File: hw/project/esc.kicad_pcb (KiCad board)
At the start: 4 copper layers, 183 parts, among them J1 Battery, J10 I2C, J11 Voltage Monitor, J12 Misc, J2 Phases, J3 FTSH-107-01-L-DV-K-A, J4 Throttle, J5 Hall, J6 Serial, J7 SPI, J8 2.54 Comm, J9 CAN, Q1 SQM50061EL_GE3, Q2 SQM50061EL_GE3, Q3 STL110N10F7, Q4 STL110N10F7, Q5 STL110N10F7, Q6 STL110N10F7, Q7 STL110N10F7, Q8 STL110N10F7, SW1 BOOT0, SW2 RESET, SW3 USER, U1 STSPIN32G4, U2 LMR51610XDBVR, U3 ATA6561-GAQW-N, X1 32MHZ 10PF

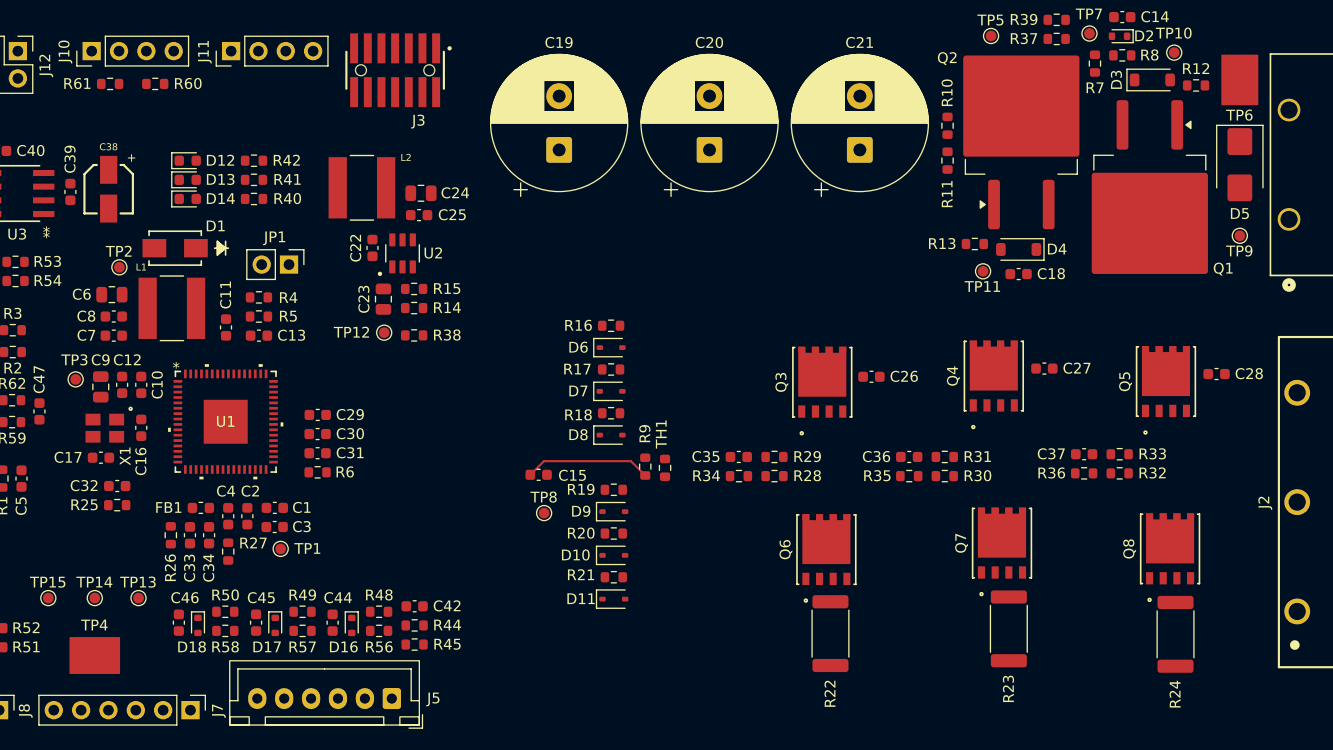
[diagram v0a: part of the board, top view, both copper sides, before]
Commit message: Rough draft layout for mosfets
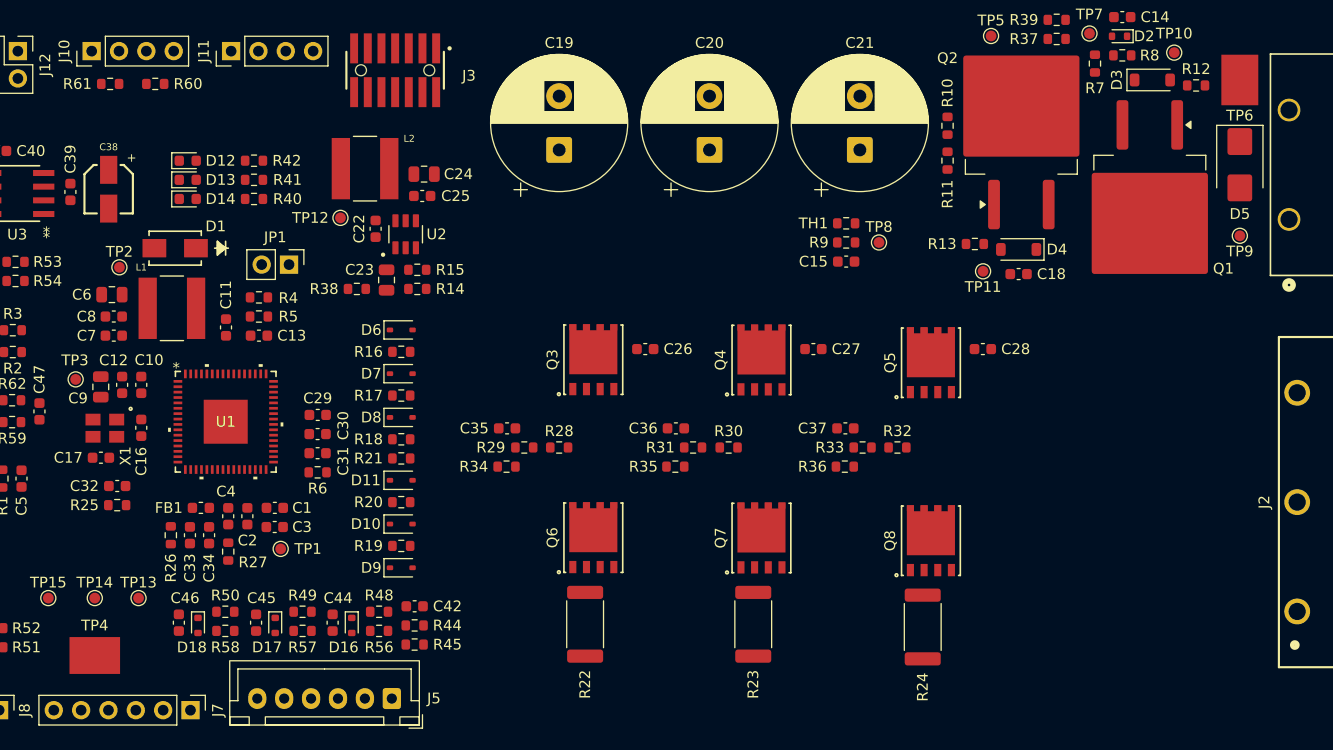
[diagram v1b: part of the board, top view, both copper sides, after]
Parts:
- moved TP8 40.0 mm to (113.3, 33.5)
- moved C15 34.8 mm to (110.2, 35.3), turned to 0 degrees
- moved TH1 28.3 mm to (110.2, 31.8), turned to 0 degrees
- moved R9 28.0 mm to (110.2, 33.5), turned to 180 degrees
- moved R33 23.9 mm to (111.8, 52.6)
- moved R23 23.8 mm to (101.6, 69.0)
- moved R24 23.5 mm to (117.3, 69.3)
- moved R31 23.4 mm to (96.0, 52.6)
- moved R29 23.3 mm to (80.3, 52.6)
- moved R22 22.8 mm to (86.0, 69.0)
- moved D11 22.6 mm to (68.9, 55.6)
- moved R21 22.6 mm to (68.9, 53.6)
- moved Q7 22.4 mm to (102.4, 61.0)
- moved C37 22.3 mm to (110.2, 50.8)
- moved R36 22.2 mm to (110.1, 54.4)
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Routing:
- net /Control/PCB_TEMP: track 11.8 -> 0.00 mm

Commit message: Rotate some parts in drive section
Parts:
- moved TP7 50.6 mm to (83.5, 3.05)
- moved D2 50.6 mm to (86.3, 3.30)
- moved R7 50.6 mm to (84.0, 5.84)
- moved C14 50.6 mm to (86.6, 1.52)
- moved R8 50.6 mm to (86.6, 5.08)
- moved R10 42.7 mm to (78.2, 33.2)
- moved R11 42.7 mm to (78.2, 36.5)
- moved C28 37.1 mm to (86.3, 37.5), turned to -90 degrees
- moved C35 34.3 mm to (93.7, 81.7), turned to -90 degrees
- moved R34 33.1 mm to (97.2, 81.7), turned to 90 degrees
- moved R29 31.4 mm to (95.4, 80.1), turned to -90 degrees
- moved Q5 30.6 mm to (87.6, 42.3), turned to 180 degrees
- moved R37 29.8 mm to (101.3, 5.84)
- moved R39 29.8 mm to (101.3, 4.06)
- moved C15 29.6 mm to (113.3, 5.84)
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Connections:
- J1 pad 1: /Peripherals/VM_IN -> PGND
- J1 pad 2: /Peripherals/VM_IN -> PGND
- J1 pad 3: PGND -> /Peripherals/VM_IN
- J1 pad 4: PGND -> /Peripherals/VM_IN
- J2 pad 1: /Drive/U -> /Drive/W
- J2 pad 3: /Drive/W -> /Drive/U
- J2 pad A1: /Drive/U -> /Drive/W
- J2 pad A3: /Drive/W -> /Drive/U
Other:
- board outline added: 150 x 75 mm

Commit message: Checkpoint before exp. with VM_IN layout
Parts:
- moved R53 60.7 mm to (-27.7, 34.8)
- moved R54 60.7 mm to (-27.7, 36.6)
- moved D21 60.7 mm to (-33.8, 34.8)
- moved D22 60.7 mm to (-33.8, 36.6)
- moved TP15 58.5 mm to (-16.5, 97.3)
- moved TP13 58.5 mm to (-8.13, 97.3)
- moved TP14 58.5 mm to (-12.2, 97.3)
- moved TP4 58.0 mm to (-11.9, 101.9)
- moved D19 56.1 mm to (-30.4, 81.3)
- moved D20 56.1 mm to (-30.4, 79.5)
- moved R51 56.1 mm to (-24.2, 81.3)
- moved R52 56.1 mm to (-24.2, 79.5)
- moved R19 41.7 mm to (103.4, 38.3), turned to -90 degrees
- moved D9 41.2 mm to (101.3, 38.3), turned to -90 degrees
- moved TP6 40.7 mm to (116.6, 38.1), turned to 180 degrees
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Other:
- board size 150 x 75 mm -> 135 x 75 mm
- board text added: "SAMPLE"

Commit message: Lock down power stuff
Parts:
- moved R10 30.1 mm to (92.2, 15.5), turned to 180 degrees
- moved R11 28.7 mm to (88.8, 15.5), turned to 180 degrees
- moved TP9 20.0 mm to (133.3, 20.8)
- moved H2 15.0 mm to (133.3, 15.5)
- moved H4 15.0 mm to (133.3, 83.3)
- moved TP10 12.2 mm to (112.3, 26.4)
- moved R12 11.7 mm to (111.3, 16.8), turned to 90 degrees
- moved J1 11.0 mm to (116.8, 41.7)
- moved J2 10.5 mm to (121.9, 64.0)
- moved D9 10.5 mm to (91.2, 35.8)
- moved Q6 10.5 mm to (88.6, 40.8)
- moved R19 10.5 mm to (93.2, 35.8)
- moved R22 10.5 mm to (96.7, 41.4)
- moved D5 10.4 mm to (112.3, 32.9)
- moved D10 10.2 mm to (91.2, 54.3)
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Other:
- board size 135 x 75 mm -> 125 x 75 mm

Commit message: errthing inside
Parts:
- moved TP4 80.5 mm to (66.3, 83.1)
- moved R9 79.2 mm to (66.3, 67.8), turned to -90 degrees
- moved TP8 79.2 mm to (68.3, 67.0), turned to 180 degrees
- moved C15 78.9 mm to (64.5, 67.8), turned to 90 degrees
- moved D19 68.6 mm to (37.5, 71.1)
- moved D20 68.6 mm to (37.5, 69.3)
- moved R51 68.6 mm to (43.7, 71.1)
- moved R52 68.6 mm to (43.7, 69.3)
- moved D21 68.4 mm to (34.5, 32.3)
- moved D22 68.4 mm to (34.5, 34.0)
- moved R53 68.4 mm to (40.6, 32.3)
- moved R54 68.4 mm to (40.6, 34.0)
- moved TP15 61.1 mm to (42.2, 80.3), turned to 90 degrees
- moved TP14 56.4 mm to (42.2, 82.3), turned to 90 degrees
- moved TP13 51.9 mm to (42.2, 84.3), turned to 90 degrees
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
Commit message: Label JST connectors
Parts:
- TP13: value HA -> HC
- TP15: value HC -> HA
- moved D19 45.8 mm to (-8.13, 67.6)
- moved D20 45.8 mm to (-8.13, 65.8)
- moved R51 45.8 mm to (-1.97, 67.6)
- moved R52 45.8 mm to (-1.97, 65.8)
- moved C33 6.30 mm to (55.4, 64.0)
- moved R25 6.30 mm to (48.7, 61.2)
- moved R26 6.30 mm to (53.6, 64.0)
- moved C15 6.30 mm to (67.6, 62.4)
- moved C29 6.30 mm to (67.3, 52.8)
- moved C34 6.30 mm to (57.2, 64.0)
- moved R27 6.30 mm to (59.0, 65.5)
- moved C11 6.30 mm to (58.8, 44.7)
- moved C12 6.30 mm to (49.1, 50.0)
- moved C13 6.30 mm to (61.8, 45.5)
- moved C32 6.30 mm to (48.7, 59.4)
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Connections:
- C44 pad 2: /Control/HA -> /Control/HC
- C46 pad 2: /Control/HC -> /Control/HA
- D16 pad 2: /Control/HA -> /Control/HC
- D18 pad 2: /Control/HC -> /Control/HA
- R56 pad 2: /Control/HA -> /Control/HC
- R58 pad 2: /Control/HC -> /Control/HA
- TP13 pad 1: /Control/HA -> /Control/HC
- TP15 pad 1: /Control/HC -> /Control/HA
- U1 pad 13: /Control/HA -> /Control/HC
- U1 pad 15: /Control/HC -> /Control/HA
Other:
- board text added: "-"
- board text added: "5V"
- board text added: "A"
- board text added: "ADC"
- board text added: "B"
- board text added: "C"
- board text added: "CANH"
- board text added: "CANL"
- board text added: "GND"
- board text added: "HA"
- board text added: "HB"
- board text added: "HC"
- board text added: "RX"
- board text added: "T"
- board text added: "TMP"
- board text added: "TX"
- board text added: "U"
- board text added: "V"
- board text added: "V+"
- board text added: "VM+"
- board text added: "VM-"
- board text added: "W"
- board text removed: "SAMPLE"

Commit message: Label everythangg
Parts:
- added TP16: CANL, TestPoint:TestPoint_Pad_D1.0mm, F.Cu at (29.7, 34.0)
- added TP17: CANH, TestPoint:TestPoint_Pad_D1.0mm, F.Cu at (29.7, 42.2)
- TP13: value HC -> HA
- TP15: value HA -> HC
- moved TP4 63.7 mm to (38.4, 27.7)
- moved D19 40.1 mm to (29.7, 80.6)
- moved D20 40.0 mm to (29.7, 78.6)
- moved R52 40.0 mm to (35.8, 80.6)
- moved R53 39.9 mm to (35.8, 78.6)
- moved R10 36.4 mm to (61.0, 22.2)
- moved R11 35.6 mm to (61.0, 18.7), turned to 90 degrees
- moved TP5 25.1 mm to (120.4, 15.0), turned to 0 degrees
- moved TP13 24.7 mm to (67.1, 79.7), turned to 180 degrees
- moved R55 18.2 mm to (38.9, 48.8)
- moved C46 18.2 mm to (57.3, 75.7)
- moved D18 18.2 mm to (59.1, 75.9)
- moved R50 18.2 mm to (61.6, 74.7)
- moved R58 18.2 mm to (61.6, 76.4)
- moved D22 18.0 mm to (35.5, 48.8)
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- renumbered J12 to J11, J11 to J12, J8 to J7, J7 to J8, R56 to R51, R51 to R52, R52 to R53, R53 to R54, R54 to R55, R55 to R56
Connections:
- C42 pad 1: Net-(J5-Pin_1) -> Net-(J5-Pin_6)
- C44 pad 2: /Control/HC -> /Control/HA
- C46 pad 2: /Control/HA -> /Control/HC
- D16 pad 2: /Control/HC -> /Control/HA
- D18 pad 2: /Control/HA -> /Control/HC
- J10 pad 1: VDD -> GND
- J10 pad 4: GND -> VDD
- J12 pad 1: VCC -> GND
- J12 pad 2: 5V -> VDD
- J12 pad 3: VDD -> 5V
- J12 pad 4: GND -> VCC
- J4 pad 1: 5V -> GND
- J4 pad 3: GND -> 5V
- J5 pad 1: Net-(J5-Pin_1) -> GND
- J5 pad 6: GND -> Net-(J5-Pin_6)
- J6 pad 1: 5V -> GND
- J6 pad 4: GND -> 5V
- J7 pad 1: 5V -> GND
- J7 pad 5: GND -> 5V
- J8 pad 1: 5V -> GND
- J8 pad 6: GND -> 5V
- J9 pad 1: 5V -> GND
- J9 pad 4: GND -> 5V
- R44 pad 2: Net-(J5-Pin_1) -> Net-(J5-Pin_6)
- R45 pad 2: Net-(J5-Pin_1) -> Net-(J5-Pin_6)
- R48 pad 2: Net-(J5-Pin_3) -> Net-(J5-Pin_5)
- R50 pad 2: Net-(J5-Pin_5) -> Net-(J5-Pin_3)
- R51 pad 1: Net-(J5-Pin_3) -> Net-(J5-Pin_5)
- R51 pad 2: /Control/HC -> /Control/HA
- R58 pad 1: Net-(J5-Pin_5) -> Net-(J5-Pin_3)
- R58 pad 2: /Control/HA -> /Control/HC
- R60 pad 1: /Control/SCL -> /Control/SDA
- R61 pad 1: /Control/SDA -> /Control/SCL
- TP13 pad 1: /Control/HC -> /Control/HA
- TP15 pad 1: /Control/HA -> /Control/HC
- U1 pad 13: /Control/HC -> /Control/HA
- U1 pad 15: /Control/HA -> /Control/HC
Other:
- board size 125 x 75 mm -> 125 x 80 mm
- board text added: "3V3"
- board text added: "BOOT"
- board text added: "FAULT"
- board text added: "MISO"
- board text added: "MOSI"
- board text added: "NSS"
- board text added: "READY"
- board text added: "RESET"
- board text added: "SCK"
- board text added: "STAT1"
- board text added: "STAT2"
- board text added: "TEMP"
- board text added: "USER"
- board text added: "VM"
- board text removed: "-"
- board text removed: "A"
- board text removed: "B"
- board text removed: "C"
- board text removed: "T"
- board text removed: "TMP"

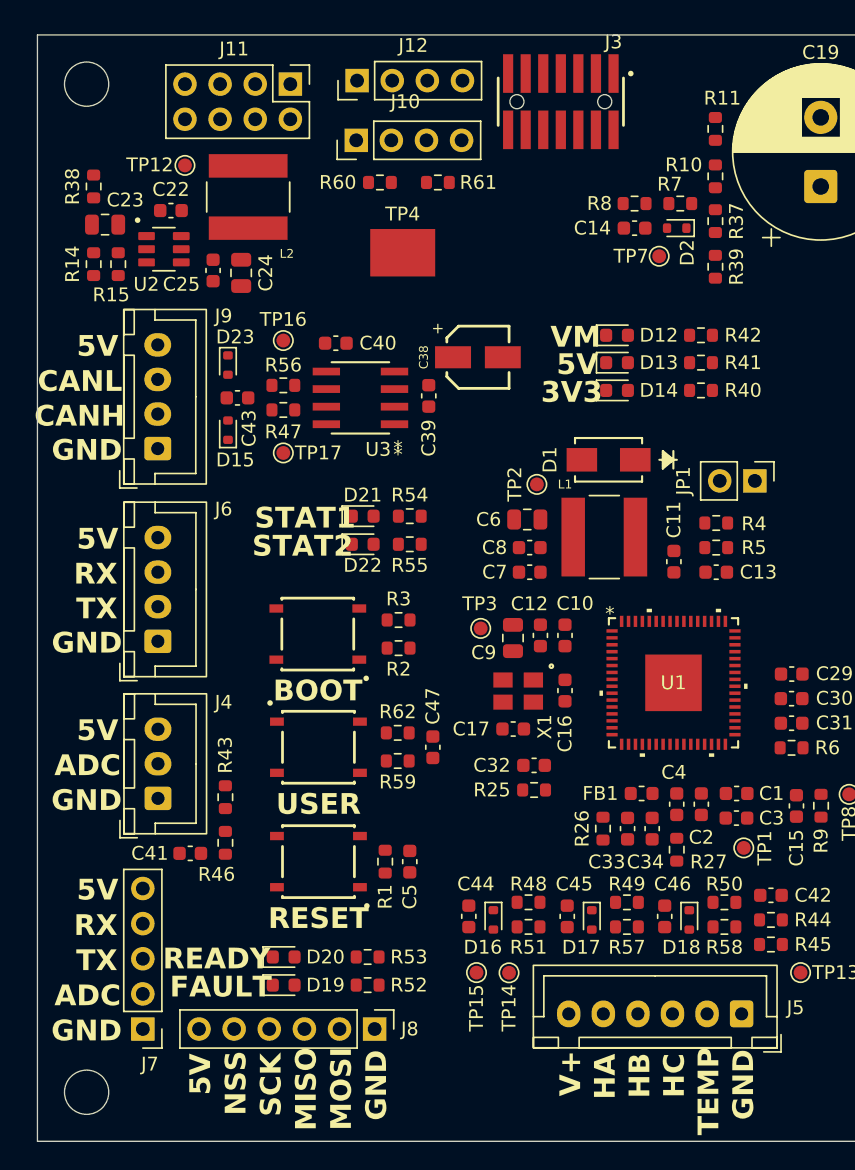
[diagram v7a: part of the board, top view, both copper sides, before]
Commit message: Lay out all subsections
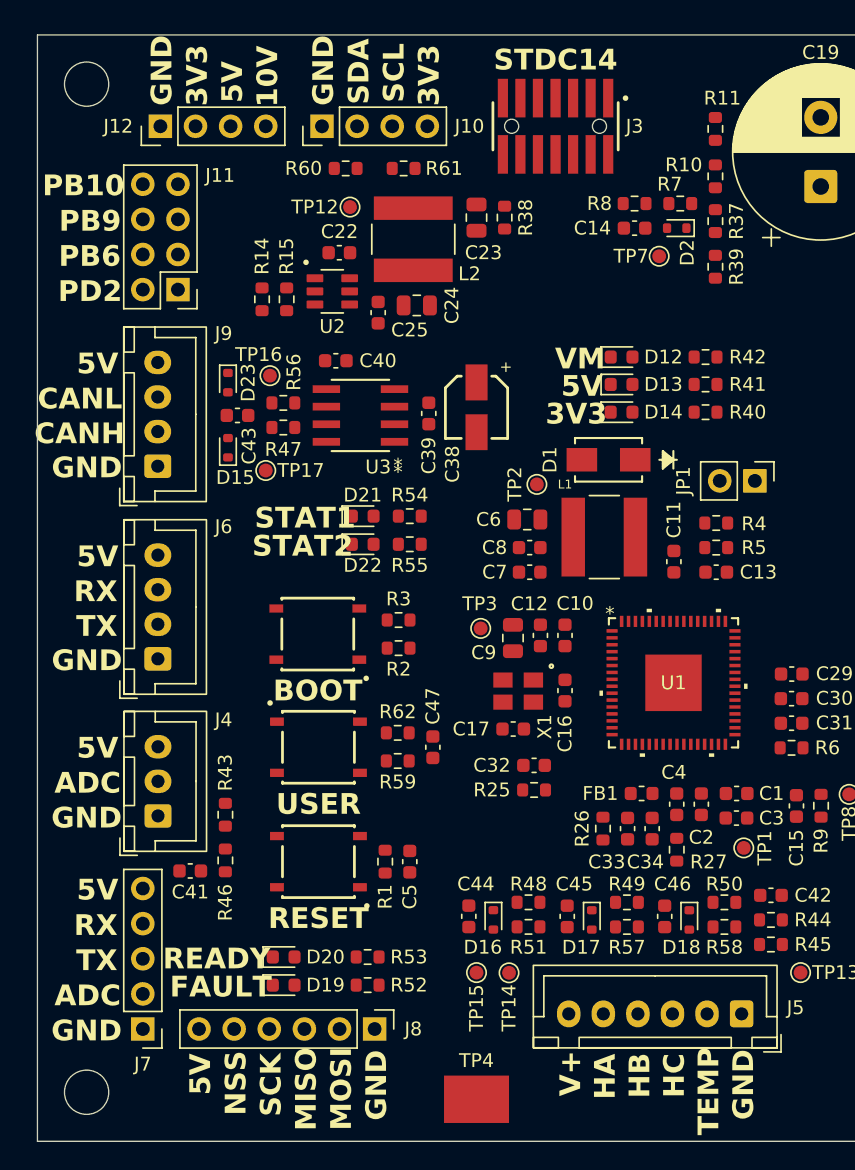
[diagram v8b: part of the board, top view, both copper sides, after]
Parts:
- moved TP4 61.4 mm to (43.7, 88.9)
- moved R38 29.8 mm to (45.7, 25.1), turned to -90 degrees
- moved C23 26.9 mm to (43.7, 25.1), turned to 90 degrees
- moved J11 16.9 mm to (22.1, 30.4), turned to 180 degrees
- moved J12 14.6 mm to (20.8, 18.5)
- moved C24 12.9 mm to (39.4, 31.5), turned to 0 degrees
- moved C22 12.6 mm to (33.8, 27.7)
- moved U2 12.6 mm to (33.3, 30.5)
- moved R14 12.4 mm to (28.2, 31.1)
- moved R15 12.4 mm to (30.0, 31.1)
- moved L2 12.3 mm to (39.1, 26.7)
- moved C25 12.3 mm to (36.6, 32.0)
- moved TP12 12.3 mm to (34.5, 24.4)
- moved C38 3.62 mm to (43.7, 38.9), turned to 90 degrees
- moved TP16 2.72 mm to (28.8, 36.6)
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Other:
- board text added: "10V"
- board text added: "PB10"
- board text added: "PB6"
- board text added: "PB9"
- board text added: "PD2"
- board text added: "SCL"
- board text added: "SDA"
- board text added: "STDC14"
